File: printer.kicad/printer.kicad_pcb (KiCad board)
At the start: 2 copper layers, 74 x 47 mm, 34 parts, among them J1 ZX_Spectrum_128K_expansion, J2 Conn_01x06_Male, J3 Conn_01x05_Male, J4 Conn_01x04_Male, U1 SN74AHC373, U2 SN74HCT00, U3 SN74AHCT02, U4 SN74AHC373, U5 XC6206PxxxMR, U6 STM32F103C8Tx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

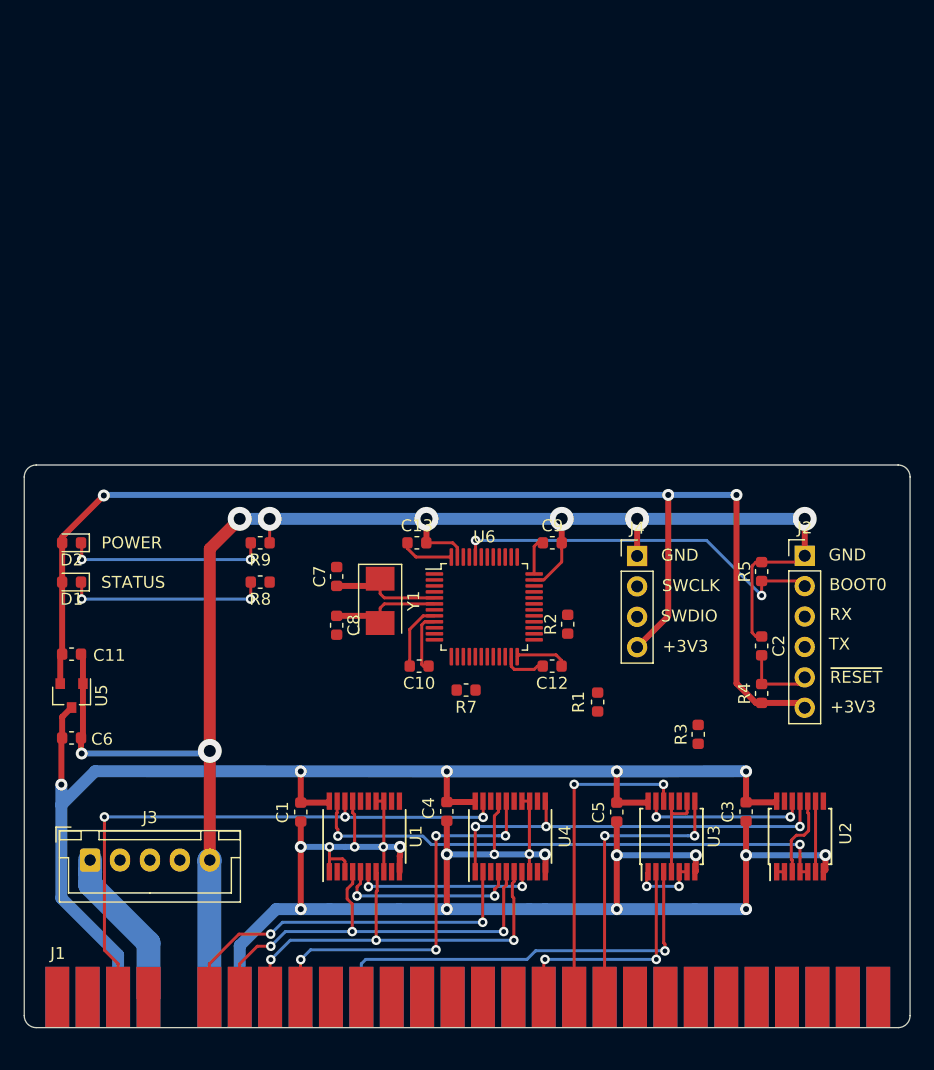
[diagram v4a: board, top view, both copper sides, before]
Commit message: Remove all ground tracks
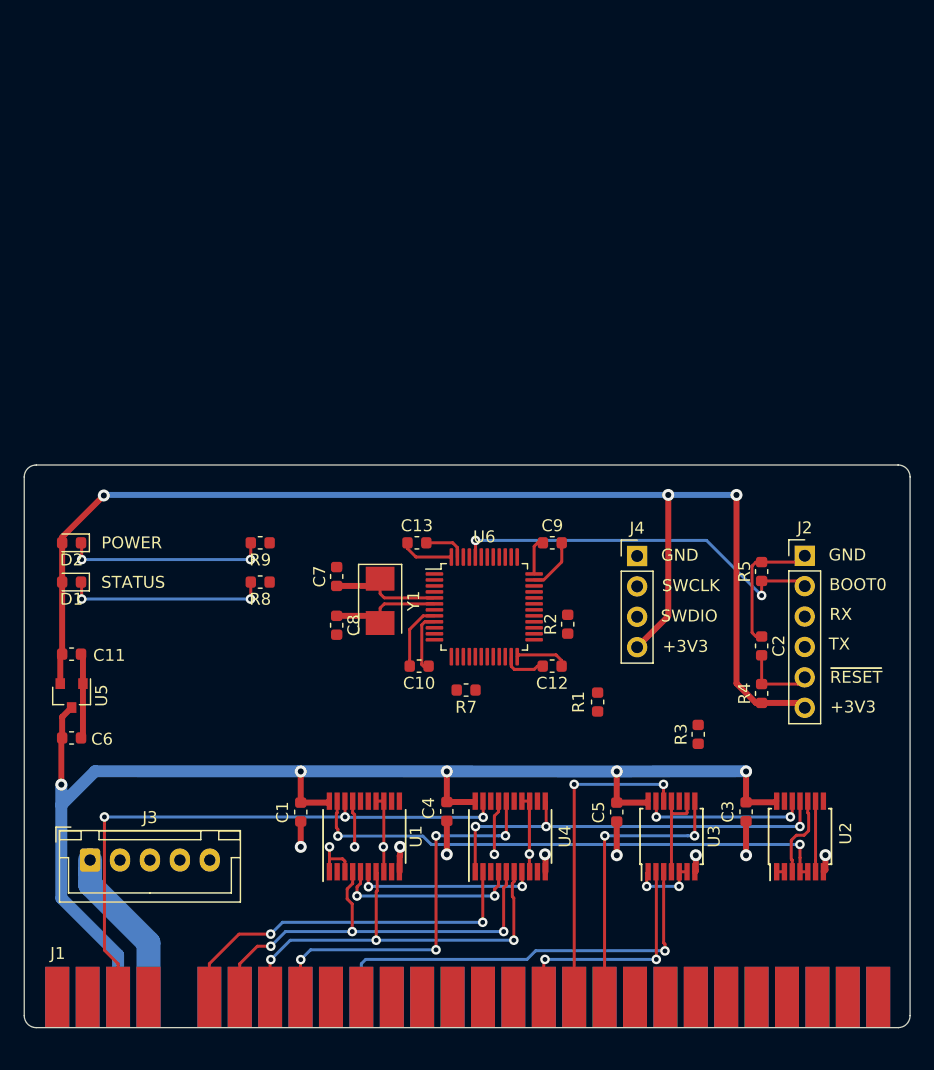
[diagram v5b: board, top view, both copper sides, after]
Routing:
- net GND: track 287.7 -> 78.9 mm, vias 25 -> 13
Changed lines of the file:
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@@
     (thickness 1.6)
     (drawings 20)
-    (tracks 427)
+    (tracks 371)
     (zones 0)
     (modules 34)
@@
   (gr_line (start 182 80) (end 110 80) (layer Edge.Cuts) (width 0.05))
   (gr_line (start 182 127) (end 110 127) (layer Edge.Cuts) (width 0.05))
-  (segment (start 124.46 113.04) (end 124.5 113) (width 2) (layer B.Cu) (net 1))
-  (segment (start 124.46 124.46) (end 124.46 113.04) (width 2) (layer B.Cu) (net 1))
-  (segment (start 127 120.146692) (end 130.046692 117.1) (width 1) (layer B.Cu) (net 1))
-  (segment (start 127 124.46) (end 127 120.146692) (width 1) (layer B.Cu) (net 1))
-  (segment (start 134.5 117.1) (end 140.3 117.1) (width 1) (layer B.Cu) (net 1))
-  (segment (start 151.2 117.1) (end 152.5 117.1) (width 1) (layer B.Cu) (net 1))
-  (segment (start 130.046692 117.1) (end 132.1 117.1) (width 1) (layer B.Cu) (net 1))
-  (segment (start 132.1 117.1) (end 134.5 117.1) (width 1) (layer B.Cu) (net 1))
-  (via (at 132.1 117.1) (size 1) (drill 0.5) (layers F.Cu B.Cu) (net 1))
-  (via (at 132.1 111.9) (size 1) (drill 0.5) (layers F.Cu B.Cu) (net 1))
-  (segment (start 132.1 111.9) (end 132.1 117.1) (width 0.5) (layer F.Cu) (net 1))
   (via (at 134.5 111.9) (size 0.8) (drill 0.4) (layers F.Cu B.Cu) (net 1))
   (segment (start 134.489 111.911) (end 134.5 111.9) (width 0.25) (layer F.Cu) (net 1))
-  (segment (start 132.1 111.9) (end 134.5 111.9) (width 0.5) (layer B.Cu) (net 1))
-  (segment (start 134.5 111.9) (end 135.8 111.9) (width 0.5) (layer B.Cu) (net 1))
   (via (at 139 111.9) (size 0.8) (drill 0.4) (layers F.Cu B.Cu) (net 1))
   (segment (start 139.039 111.861) (end 139 111.9) (width 0.25) (layer F.Cu) (net 1))
@@
   (segment (start 138.389 108.08) (end 139.039 108.08) (width 0.25) (layer F.Cu) (net 1))
   (via (at 136.6 111.9) (size 0.8) (drill 0.4) (layers F.Cu B.Cu) (net 1))
-  (segment (start 135.8 111.9) (end 136.6 111.9) (width 0.5) (layer B.Cu) (net 1))
-  (segment (start 136.6 111.9) (end 139 111.9) (width 0.5) (layer B.Cu) (net 1))
   (segment (start 135.789 113.98) (end 135.789 113.094998) (width 0.25) (layer F.Cu) (net 1))
   (segment (start 134.489 113.98) (end 134.5 112.9) (width 0.25) (layer F.Cu) (net 1))
@@
   (segment (start 139.039 111.939) (end 139 111.9) (width 0.25) (layer F.Cu) (net 1))
   (segment (start 139.039 113.98) (end 139.039 111.939) (width 0.25) (layer F.Cu) (net 1))
-  (via (at 144.3 117.1) (size 1) (drill 0.5) (layers F.Cu B.Cu) (net 1))
-  (segment (start 140.3 117.1) (end 144.3 117.1) (width 1) (layer B.Cu) (net 1))
-  (segment (start 144.3 117.1) (end 151.2 117.1) (width 1) (layer B.Cu) (net 1))
   (segment (start 150.573 108.08) (end 151.223 108.08) (width 0.25) (layer F.Cu) (net 1))
   (via (at 144.3 112.525) (size 1) (drill 0.5) (layers F.Cu B.Cu) (net 1))
   (segment (start 144.3 112.6) (end 144.3 112.525) (width 0.5) (layer F.Cu) (net 1))
-  (segment (start 144.3 112.6) (end 144.3 117.1) (width 0.5) (layer F.Cu) (net 1))
   (via (at 152.5 112.525) (size 1) (drill 0.5) (layers F.Cu B.Cu) (net 1))
   (segment (start 152.548001 112.894999) (end 152.548001 113.98) (width 0.5) (layer F.Cu) (net 1))
@@
   (via (at 151.2 112.5) (size 0.8) (drill 0.4) (layers F.Cu B.Cu) (net 1))
   (segment (start 151.225 112.525) (end 151.2 112.5) (width 0.25) (layer B.Cu) (net 1))
-  (segment (start 151.225 112.525) (end 152.5 112.525) (width 0.5) (layer B.Cu) (net 1))
   (segment (start 151.2 113.957) (end 151.223 113.98) (width 0.25) (layer F.Cu) (net 1))
   (segment (start 151.2 112.5) (end 151.2 113.957) (width 0.25) (layer F.Cu) (net 1))
   (segment (start 151.2 108.103) (end 151.223 108.08) (width 0.25) (layer F.Cu) (net 1))
   (segment (start 151.2 112.5) (end 151.2 108.103) (width 0.25) (layer F.Cu) (net 1))
-  (segment (start 144.3 112.525) (end 148.275 112.525) (width 0.5) (layer B.Cu) (net 1))
-  (segment (start 148.275 112.525) (end 151.225 112.525) (width 0.5) (layer B.Cu) (net 1))
   (via (at 148.275 112.525) (size 0.8) (drill 0.4) (layers F.Cu B.Cu) (net 1))
   (segment (start 148.623 108.965002) (end 148.623 108.08) (width 0.25) (layer F.Cu) (net 1))
@@
   (segment (start 148.275 112.525) (end 148.275 109.313002) (width 0.25) (layer F.Cu) (net 1))
   (via (at 140.4 111.9) (size 1) (drill 0.5) (layers F.Cu B.Cu) (net 1))
-  (segment (start 139 111.9) (end 140.4 111.9) (width 0.5) (layer B.Cu) (net 1))
   (segment (start 140.364001 112.643105) (end 140.364001 113.98) (width 0.5) (layer F.Cu) (net 1))
   (segment (start 140.4 111.9) (end 140.4 112.607106) (width 0.5) (layer F.Cu) (net 1))
   (segment (start 140.4 112.607106) (end 140.364001 112.643105) (width 0.5) (layer F.Cu) (net 1))
-  (via (at 158.5 117.1) (size 1) (drill 0.5) (layers F.Cu B.Cu) (net 1))
-  (segment (start 152.5 117.1) (end 158.5 117.1) (width 1) (layer B.Cu) (net 1))
-  (segment (start 158.5 117.1) (end 165 117.1) (width 1) (layer B.Cu) (net 1))
-  (segment (start 158.5 112.6) (end 158.5 117.1) (width 0.5) (layer F.Cu) (net 1))
   (via (at 158.5 112.6) (size 1) (drill 0.5) (layers F.Cu B.Cu) (net 1))
   (via (at 165.1 112.6) (size 1) (drill 0.5) (layers F.Cu B.Cu) (net 1))
-  (segment (start 158.5 112.6) (end 165.1 112.6) (width 0.5) (layer B.Cu) (net 1))
   (segment (start 165.1 113.923001) (end 165.043001 113.98) (width 0.5) (layer F.Cu) (net 1))
   (segment (start 165.1 112.6) (end 165.1 113.923001) (width 0.5) (layer F.Cu) (net 1))
-  (via (at 169.3 117.1) (size 1) (drill 0.5) (layers F.Cu B.Cu) (net 1))
-  (segment (start 165 117.1) (end 169.3 117.1) (width 1) (layer B.Cu) (net 1))
-  (segment (start 169.3 112.6) (end 169.3 117.1) (width 0.5) (layer F.Cu) (net 1))
   (via (at 169.3 112.6) (size 1) (drill 0.5) (layers F.Cu B.Cu) (net 1))
   (via (at 175.931 112.589179) (size 1) (drill 0.5) (layers F.Cu B.Cu) (net 1))
-  (segment (start 169.3 112.6) (end 175.920179 112.6) (width 0.5) (layer B.Cu) (net 1))
   (segment (start 175.920179 112.6) (end 175.931 112.589179) (width 0.5) (layer B.Cu) (net 1))
   (segment (start 175.931 113.830001) (end 175.781001 113.98) (width 0.5) (layer F.Cu) (net 1))
   (segment (start 175.931 112.589179) (end 175.931 113.830001) (width 0.5) (layer F.Cu) (net 1))
   (segment (start 144.3 109.728) (end 144.3 112.6) (width 0.5) (layer F.Cu) (net 1))
-  (segment (start 132.1 109.779) (end 132.1 111.9) (width 0.5) (layer F.Cu) (net 1))
   (segment (start 169.3 109.7535) (end 169.3 112.6) (width 0.5) (layer F.Cu) (net 1))
   (segment (start 158.496 109.779) (end 158.5 112.6) (width 0.5) (layer F.Cu) (net 1))
@@
   (segment (start 173.6675 88.1125) (end 174.2 87.58) (width 0.25) (layer F.Cu) (net 1))
   (segment (start 170.6 88.1125) (end 173.6675 88.1125) (width 0.25) (layer F.Cu) (net 1))
-  (segment (start 124.5 113) (end 124.5 87) (width 1) (layer F.Cu) (net 1))
-  (segment (start 124.5 87) (end 127 84.5) (width 1) (layer F.Cu) (net 1))
-  (via (at 127 84.5) (size 2) (drill 1) (layers F.Cu B.Cu) (net 1))
-  (via (at 174.2 84.5) (size 2) (drill 1) (layers F.Cu B.Cu) (net 1))
-  (segment (start 174.2 84.5) (end 174.2 87.58) (width 0.5) (layer F.Cu) (net 1))
-  (via (at 160.2 84.5) (size 2) (drill 1) (layers F.Cu B.Cu) (net 1))
-  (segment (start 160.2 84.5) (end 174.2 84.5) (width 1) (layer B.Cu) (net 1))
-  (segment (start 160.2 84.5) (end 160.2 87.6) (width 0.5) (layer F.Cu) (net 1))
-  (via (at 153.9 84.5) (size 2) (drill 1) (layers F.Cu B.Cu) (net 1))
-  (segment (start 153.9 84.5) (end 160.2 84.5) (width 1) (layer B.Cu) (net 1))
-  (segment (start 153.9 84.5) (end 153.9 86.5) (width 0.5) (layer F.Cu) (net 1))
-  (via (at 142.6 84.5) (size 2) (drill 1) (layers F.Cu B.Cu) (net 1))
-  (segment (start 142.6 84.5) (end 153.9 84.5) (width 1) (layer B.Cu) (net 1))
-  (segment (start 142.6 86.4875) (end 142.5875 86.5) (width 0.5) (layer F.Cu) (net 1))
-  (segment (start 142.6 84.5) (end 142.6 86.4875) (width 0.5) (layer F.Cu) (net 1))
-  (segment (start 129.5 84.5) (end 142.6 84.5) (width 1) (layer B.Cu) (net 1))
-  (via (at 129.5 84.5) (size 2) (drill 1) (layers F.Cu B.Cu) (net 1))
-  (segment (start 127 84.5) (end 129.5 84.5) (width 1) (layer B.Cu) (net 1))
-  (segment (start 129.5 84.5) (end 129.5 86.5) (width 0.25) (layer F.Cu) (net 1))
-  (via (at 113.8 104.1) (size 1) (drill 0.5) (layers F.Cu B.Cu) (net 1))
-  (segment (start 113.7435 102.8) (end 113.7435 104.0435) (width 0.5) (layer F.Cu) (net 1))
-  (segment (start 113.7435 104.0435) (end 113.8 104.1) (width 0.5) (layer F.Cu) (net 1))
-  (via (at 124.500053 103.884395) (size 2) (drill 1) (layers F.Cu B.Cu) (net 1))
-  (segment (start 113.8 104.1) (end 124.284448 104.1) (width 0.5) (layer B.Cu) (net 1))
-  (segment (start 124.284448 104.1) (end 124.500053 103.884395) (width 0.5) (layer B.Cu) (net 1))
   (segment (start 170.125 94.325) (end 170.6 94.325) (width 0.25) (layer F.Cu) (net 1))
   (segment (start 169.79999 88.43751) (end 169.79999 93.99999) (width 0.25) (layer F.Cu) (net 1))
@@
   (segment (start 169.79999 93.99999) (end 170.125 94.325) (width 0.25) (layer F.Cu) (net 1))
   (segment (start 170.6 88.1125) (end 170.125 88.1125) (width 0.25) (layer F.Cu) (net 1))
+  (segment (start 132.1 109.779) (end 132.1 111.9) (width 0.5) (layer F.Cu) (net 1))
+  (via (at 132.1 111.9) (size 1) (drill 0.5) (layers F.Cu B.Cu) (net 1))
   (segment (start 134.339999 108.204) (end 134.463999 108.08) (width 0.5) (layer F.Cu) (net 2))
   (segment (start 132.1 108.204) (end 134.339999 108.204) (width 0.5) (layer F.Cu) (net 2))

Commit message: Routed all connections, with ground fill
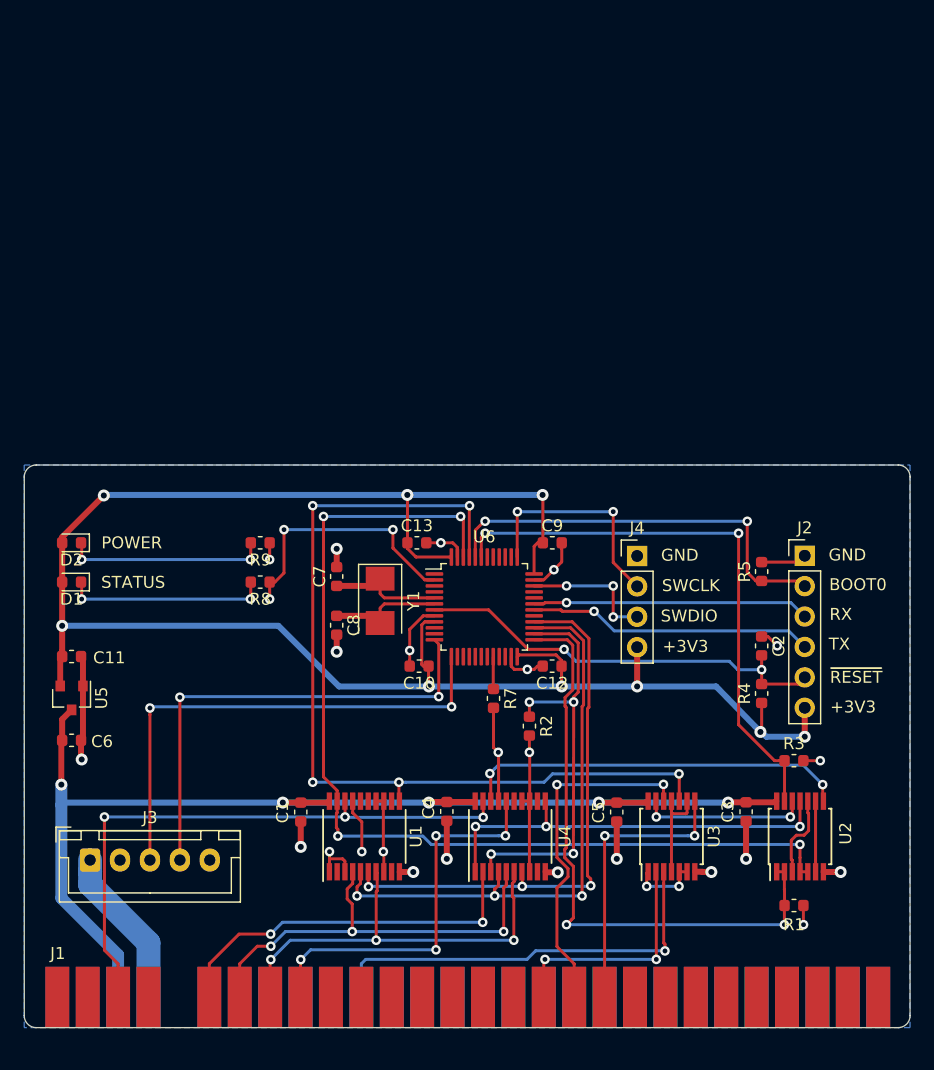
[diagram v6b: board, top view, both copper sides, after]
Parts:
- moved R1 23.6 mm to (173.3, 116.8), turned to 0 degrees
- moved R2 9.09 mm to (151.2, 101.8), turned to 270 degrees
- moved R3 8.30 mm to (173.3, 104.7), turned to 0 degrees
- moved R7 2.39 mm to (148.2, 99.5), turned to 270 degrees
- moved C11 0.20 mm to (113.0, 96.0)
- moved C6 0.20 mm to (113.0, 103.0)
- moved U5 0.20 mm to (113.0, 99.5)
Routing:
- net /WRITE: track 0.00 -> 75.3 mm, vias 0 -> 5
- net /PAPER: track 0.65 -> 51.0 mm, vias 0 -> 2
- net /READY: track 0.00 -> 47.8 mm, vias 0 -> 2
- net /PRINTER_RX: track 0.00 -> 42.1 mm, vias 0 -> 2
- net /PRINTER_TX: track 0.00 -> 40.1 mm, vias 0 -> 2
- net /STYLUS: track 44.8 -> 84.0 mm, vias 2 -> 4
- net /ENCODER: track 0.00 -> 35.1 mm, vias 0 -> 4
- net +3V3: track 123.3 -> 157.3 mm, vias 3 -> 9
- net /MOTOR_SLOW: track 15.8 -> 49.2 mm, vias 2 -> 3
- net Net-(U2-Pad8): track 0.00 -> 32.5 mm, vias 0 -> 2
- net /MOTOR_OFF: track 15.4 -> 47.1 mm, vias 2 -> 3
- net /~RESET: track 6.23 -> 35.6 mm, vias 0 -> 2
- net /PROGRAM_TX: track 0.00 -> 23.9 mm, vias 0 -> 1
- net /PROGRAM_RX: track 0.00 -> 23.1 mm, vias 0 -> 1
- net /STATUS_LED: track 0.00 -> 21.8 mm, vias 0 -> 3
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- added copper zone on B.Cu, net GND

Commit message: Tidy up a bit
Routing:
- net GND: track 90.6 -> 94.5 mm
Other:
- outline, holes or cut-outs redrawn
- board text added: "PRINTER"
